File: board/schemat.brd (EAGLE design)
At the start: 69.5 x 92.7 mm, 42 parts, among them IC1 MEGA8-P, IC2 L293D, Q1 10MHz

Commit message: Adding on github
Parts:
- moved C13 52.8 mm to (53.3, 8.89), turned to 90 degrees
- moved LEFT_FEEDBACK 1.27 mm to (6.35, 24.1)
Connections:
- removed net VCC_MOTOR: IC2.8
- net VCC_MOTORS: now also IC2.8
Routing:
- net GND: track 7.62 -> 537.8 mm
- net VCC: track 0.00 -> 267.1 mm
- net BATTERY_VCC: track 0.00 -> 83.8 mm
- net LIGHT_LEFT: track 0.00 -> 69.5 mm
- net N$7: track 0.00 -> 59.3 mm
- net RIGHT2: track 0.00 -> 49.0 mm
- net LEFT2: track 0.00 -> 41.0 mm
- net VCC_BLUETOOTH: track 0.00 -> 35.3 mm
- net SCK: track 0.00 -> 35.2 mm
- net LIGHT_RIGHT: track 0.00 -> 34.9 mm
- net FRONT2: track 0.00 -> 31.8 mm
- net MISO: track 0.00 -> 29.6 mm
- net N$4: track 0.00 -> 28.2 mm
- net MOSI: track 0.00 -> 25.0 mm
- net FRONT1: track 0.00 -> 21.4 mm
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- added copper zone on layer 16, net N$1

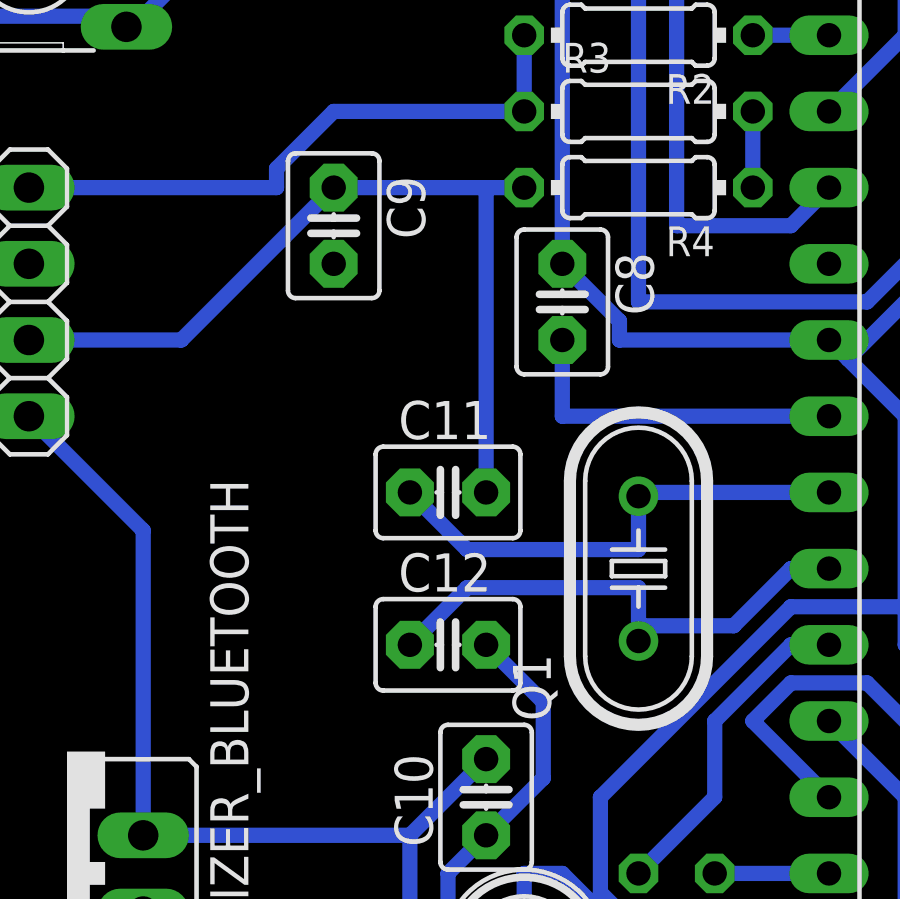
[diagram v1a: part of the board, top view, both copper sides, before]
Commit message: Fixed position of few capasitors
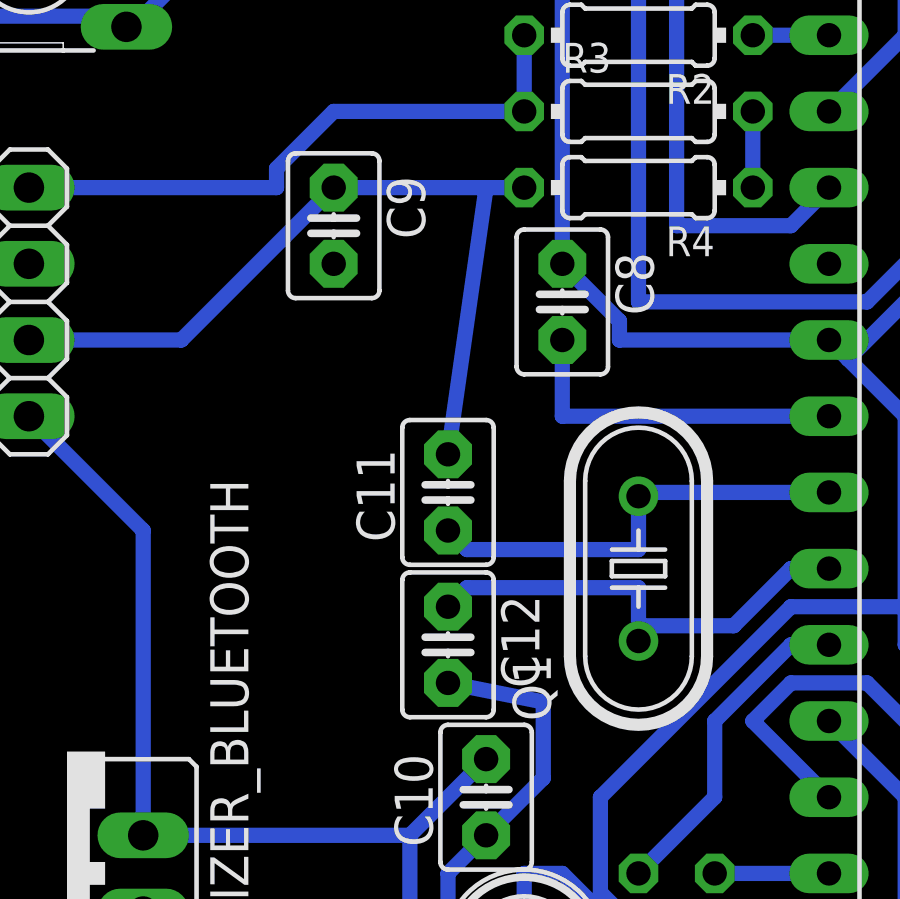
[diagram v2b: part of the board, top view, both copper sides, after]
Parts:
- turned C11 to 90 degrees
- turned C12 to 270 degrees
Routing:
- net N$12: track 17.3 -> 15.5 mm
- net N$13: track 16.7 -> 14.9 mm
- net GND: track 537.8 -> 537.2 mm
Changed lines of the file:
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@@
 <?xml version="1.0" encoding="utf-8"?>
 <!DOCTYPE eagle SYSTEM "eagle.dtd">
-<eagle version="8.6.0">
+<eagle version="8.7.1">
 <drawing>
 <settings>
@@
 <attribute name="OC_NEWARK" value="unknown" x="24.13" y="48.26" size="1.778" layer="27" rot="R90" display="off"/>
 </element>
-<element name="C11" library="capacitor-wima" library_urn="urn:adsk.eagle:library:116" package="C2.5-3" package3d_urn="urn:adsk.eagle:package:5436/1" value="22pF" x="17.78" y="50.8"/>
-<element name="C12" library="capacitor-wima" library_urn="urn:adsk.eagle:library:116" package="C2.5-3" package3d_urn="urn:adsk.eagle:package:5436/1" value="22pF" x="17.78" y="45.72"/>
+<element name="C11" library="capacitor-wima" library_urn="urn:adsk.eagle:library:116" package="C2.5-3" package3d_urn="urn:adsk.eagle:package:5436/1" value="22pF" x="17.78" y="50.8" rot="R90"/>
+<element name="C12" library="capacitor-wima" library_urn="urn:adsk.eagle:library:116" package="C2.5-3" package3d_urn="urn:adsk.eagle:package:5436/1" value="22pF" x="17.78" y="45.72" rot="R270"/>
 <element name="RIGHT_FEEDBACK" library="pinhead" library_urn="urn:adsk.eagle:library:325" package="1X03" package3d_urn="urn:adsk.eagle:package:22458/2" value="" x="58.42" y="26.67" rot="R270"/>
 <element name="LEFT_FEEDBACK" library="pinhead" library_urn="urn:adsk.eagle:library:325" package="1X03" package3d_urn="urn:adsk.eagle:package:22458/2" value="" x="6.35" y="24.13" rot="R270"/>
@@
 <wire x1="15.24" y1="30.48" x2="13.97" y2="31.75" width="0.508" layer="16"/>
 <wire x1="15.24" y1="30.48" x2="15.24" y2="30.861" width="0.508" layer="16"/>
-<wire x1="20.955" y1="43.815" x2="19.05" y2="45.72" width="0.508" layer="16"/>
+<wire x1="20.955" y1="43.815" x2="17.78" y2="44.45" width="0.508" layer="16"/>
 <wire x1="20.955" y1="41.275" x2="20.955" y2="43.815" width="0.508" layer="16"/>
 <wire x1="19.05" y1="39.37" x2="20.955" y2="41.275" width="0.508" layer="16"/>
@@
 <wire x1="13.97" y1="60.96" x2="19.05" y2="60.96" width="0.508" layer="16"/>
 <wire x1="19.05" y1="60.96" x2="20.32" y2="60.96" width="0.508" layer="16"/>
-<wire x1="19.05" y1="60.96" x2="19.05" y2="50.8" width="0.508" layer="16"/>
+<wire x1="19.05" y1="60.96" x2="17.78" y2="52.07" width="0.508" layer="16"/>
 <wire x1="0.635" y1="55.88" x2="1.27" y2="55.88" width="0.508" layer="16"/>
 <wire x1="1.27" y1="55.88" x2="3.81" y2="55.88" width="0.508" layer="16"/>
@@
 <wire x1="29.21" y1="48.26" x2="27.305" y2="46.355" width="0.508" layer="16"/>
 <wire x1="30.48" y1="48.26" x2="29.21" y2="48.26" width="0.508" layer="16"/>
-<wire x1="18.415" y1="47.625" x2="16.51" y2="45.72" width="0.508" layer="16"/>
+<wire x1="18.415" y1="47.625" x2="17.78" y2="46.99" width="0.508" layer="16"/>
 <wire x1="24.13" y1="47.625" x2="18.415" y2="47.625" width="0.508" layer="16"/>
 <wire x1="24.13" y1="46.355" x2="24.13" y2="47.625" width="0.508" layer="16"/>
@@
 <wire x1="30.48" y1="50.8" x2="24.13" y2="50.8" width="0.508" layer="16"/>
 <wire x1="24.13" y1="50.8" x2="24.13" y2="50.673" width="0.508" layer="16"/>
-<wire x1="18.415" y1="48.895" x2="16.51" y2="50.8" width="0.508" layer="16"/>
+<wire x1="18.415" y1="48.895" x2="17.78" y2="49.53" width="0.508" layer="16"/>
 <wire x1="24.13" y1="48.895" x2="18.415" y2="48.895" width="0.508" layer="16"/>
 <wire x1="24.13" y1="50.673" x2="24.13" y2="48.895" width="0.508" layer="16"/>
